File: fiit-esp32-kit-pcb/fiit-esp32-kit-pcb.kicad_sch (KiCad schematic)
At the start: 43 parts, among them J1 Conn_01x22_Pin, J2 Conn_01x22_Pin, J3 Conn_01x05_Pin, J4 Conn_01x05_Pin, J5 Conn_ARM_JTAG_SWD_10, J6 Conn_01x06_Pin, J7 QWIIC - I2C, SW5 SPST NO, U1 ESP32-S3-WROOM-1, U2 SY8089AAAC

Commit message: footprints assignment
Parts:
- removed JP1: I2C_PULL_UP, symbol Jumper:SolderJumper_3_Bridged123
- added JP1, JP2: I2C, Jumper:SolderJumper-2_P1.3mm_Bridged_RoundedPad1.0x1.5mm, symbol Jumper:SolderJumper_2_Bridged
- J1, J2: footprint (none) -> Connector_PinHeader_2.54mm:PinHeader_1x22_P2.54mm_Vertical
- J3, J4: footprint (none) -> Connector_PinHeader_2.54mm:PinHeader_1x05_P2.54mm_Vertical
- J5: footprint (none) -> Connector_IDC:IDC-Header_2x05_P2.54mm_Vertical
- J6: footprint (none) -> Connector_IDC:IDC-Header_2x03_P2.54mm_Vertical
- JP3: renamed from JP2; footprint (none) -> Jumper:SolderJumper-2_P1.3mm_Bridged_RoundedPad1.0x1.5mm
- L1: footprint Findemm:INDC2116X100N -> FIIT_Kit:INDC2116X100N
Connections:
- net +3.3V: now also JP1.2 (B), JP2.2 (B)
- net at R3.1: now also JP2.1 (A)
- net at R2.1: now also JP1.1 (A)
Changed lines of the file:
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@@
 	)
 	(junction
+		(at 246.38 110.49)
+		(diameter 0)
+		(color 0 0 0 0)
+	)
+	(junction
 		(at 163.83 168.91)
 		(diameter 0)
@@
 	(wire
 		(pts
+			(xy 238.76 113.03) (xy 238.76 110.49)
+		)
+		(stroke
+			(width 0)
+			(type default)
+		)
+	)
+	(wire
+		(pts
 			(xy 228.6 88.9) (xy 232.41 88.9)
 		)
@@
 	(wire
 		(pts
-			(xy 54.61 173.99) (xy 54.61 179.07)
+			(xy 254 113.03) (xy 254 110.49)
 		)
 		(stroke
@@
 	(wire
 		(pts
-			(xy 163.83 168.91) (xy 163.83 166.37)
+			(xy 54.61 173.99) (xy 54.61 179.07)
 		)
 		(stroke
@@
 	(wire
 		(pts
-			(xy 63.5 21.59) (xy 63.5 33.02)
+			(xy 163.83 168.91) (xy 163.83 166.37)
 		)
 		(stroke
@@
 	(wire
 		(pts
-			(xy 172.72 82.55) (xy 175.26 82.55)
+			(xy 63.5 21.59) (xy 63.5 33.02)
 		)
 		(stroke
@@
 	(wire
 		(pts
-			(xy 232.41 91.44) (xy 232.41 88.9)
+			(xy 172.72 82.55) (xy 175.26 82.55)
 		)
 		(stroke
@@
 	(wire
 		(pts
-			(xy 129.54 77.47) (xy 144.78 77.47)
+			(xy 232.41 91.44) (xy 232.41 88.9)
 		)
 		(stroke
@@
 	(wire
 		(pts
-			(xy 232.41 99.06) (xy 232.41 96.52)
+			(xy 129.54 77.47) (xy 144.78 77.47)
 		)
 		(stroke
@@
 	(wire
 		(pts
-			(xy 238.76 120.65) (xy 241.3 120.65)
+			(xy 232.41 99.06) (xy 232.41 96.52)
 		)
 		(stroke
@@
 	(wire
 		(pts
+			(xy 246.38 110.49) (xy 246.38 109.22)
+		)
+		(stroke
+			(width 0)
+			(type default)
+		)
+	)
+	(wire
+		(pts
 			(xy 142.24 29.21) (xy 144.78 29.21)
 		)
@@
 	(wire
 		(pts
+			(xy 246.38 110.49) (xy 254 110.49)
+		)
+		(stroke
+			(width 0)
+			(type default)
+		)
+	)
+	(wire
+		(pts
 			(xy 187.96 39.37) (xy 172.72 39.37)
 		)
@@
 	(wire
 		(pts
-			(xy 251.46 120.65) (xy 254 120.65)
-		)
-		(stroke
-			(width 0)
-			(type default)
-		)
-	)
-	(wire
-		(pts
 			(xy 187.96 59.69) (xy 172.72 59.69)
 		)
@@
 	(wire
 		(pts
-			(xy 246.38 115.57) (xy 246.38 116.84)
+			(xy 238.76 110.49) (xy 246.38 110.49)
 		)
 		(stroke
@@
 			)
 		)
-		(property "Footprint" "Findemm:INDC2116X100N"
+		(property "Footprint" "FIIT_Kit:INDC2116X100N"
 			(at 85.09 168.91 0)
 			(effects
@@
 	)
 	(symbol
+		(lib_id "Jumper:SolderJumper_2_Bridged")
+		(at 238.76 116.84 90)
+		(unit 1)
+		(exclude_from_sim yes)
+		(in_bom no)
+		(on_board yes)
+		(dnp no)
+		(fields_autoplaced yes)
+		(property "Reference" "JP1"
+			(at 241.3 115.5699 90)
+			(effects
+				(font
+					(size 1.27 1.27)
+				)
+				(justify right)
+			)
+		)
+		(property "Value" "I2C"
+			(at 241.3 118.1099 90)
+			(effects
+				(font
+					(size 1.27 1.27)
+				)
+				(justify right)
+			)
+		)
+		(property "Footprint" "Jumper:SolderJumper-2_P1.3mm_Bridged_RoundedPad1.0x1.5mm"
+			(at 238.76 116.84 0)
+			(effects
+				(font
+					(size 1.27 1.27)
+				)
+				(hide yes)
+			)
+		)
+		(property "Datasheet" "~"
+			(at 238.76 116.84 0)
+			(effects
+				(font
+					(size 1.27 1.27)
+				)
+				(hide yes)
+			)
+		)
+		(property "Description" "Solder Jumper, 2-pole, closed/bridged"
+			(at 238.76 116.84 0)
+			(effects
+				(font
+					(size 1.27 1.27)
+				)
+				(hide yes)
+			)
+		)
+		(pin "1"
+		)
+		(pin "2"
+		)
+		(instances
+			(project ""
+				(path "/d7013812-ce13-4db9-a6cc-42acdc5acaf9"
+					(reference "JP1")
+					(unit 1)
+				)
+			)
+		)
+	)
+	(symbol
 		(lib_id "Connector:TestPoint")
 		(at 168.91 167.64 0)
@@
 			)
 		)
-		(property "Footprint" ""
+		(property "Footprint" "Connector_PinHeader_2.54mm:PinHeader_1x22_P2.54mm_Vertical"
 			(at 167.64 54.61 0)
 			(effects
@@
 		(dnp no)
 		(fields_autoplaced yes)
-		(property "Reference" "JP2"
+		(property "Reference" "JP3"
 			(at 151.13 162.56 0)
 			(effects
@@
 			)
 		)
-		(property "Footprint" ""
+		(property "Footprint" "Jumper:SolderJumper-2_P1.3mm_Bridged_RoundedPad1.0x1.5mm"
 			(at 151.13 168.91 0)
 			(effects
@@
 			(project "fiit-esp32-kit-pcb"
 				(path "/d7013812-ce13-4db9-a6cc-42acdc5acaf9"
-					(reference "JP2")
+					(reference "JP3")
 					(unit 1)
 				)
@@
 			)
 		)
-		(property "Footprint" ""
+		(property "Footprint" "Connector_IDC:IDC-Header_2x03_P2.54mm_Vertical"
 			(at 165.1 127 0)
 			(effects
@@
 			)
 		)
-		(property "Footprint" ""
+		(property "Footprint" "Connector_PinHeader_2.54mm:PinHeader_1x22_P2.54mm_Vertical"
 			(at 149.86 54.61 0)
 			(effects
@@
 			)
 		)
-		(property "Footprint" ""
+		(property "Footprint" "Connector_PinHeader_2.54mm:PinHeader_1x05_P2.54mm_Vertical"
 			(at 223.52 93.98 0)
 			(effects
@@
 	)
 	(symbol
+		(lib_id "Jumper:SolderJumper_2_Bridged")
+		(at 254 116.84 90)
+		(unit 1)
+		(exclude_from_sim yes)
+		(in_bom no)
+		(on_board yes)
+		(dnp no)
+		(fields_autoplaced yes)
+		(property "Reference" "JP2"
+			(at 256.54 115.5699 90)
+			(effects
+				(font
+					(size 1.27 1.27)
+				)
+				(justify right)
+			)
+		)
+		(property "Value" "I2C"
+			(at 256.54 118.1099 90)
+			(effects
+				(font
+					(size 1.27 1.27)
+				)
+				(justify right)
+			)
+		)
+		(property "Footprint" "Jumper:SolderJumper-2_P1.3mm_Bridged_RoundedPad1.0x1.5mm"
+			(at 254 116.84 0)
+			(effects
+				(font
+					(size 1.27 1.27)
+				)
+				(hide yes)
+			)
+		)
+		(property "Datasheet" "~"
+			(at 254 116.84 0)
+			(effects
+				(font
+					(size 1.27 1.27)
+				)
+				(hide yes)
+			)
+		)
+		(property "Description" "Solder Jumper, 2-pole, closed/bridged"
+			(at 254 116.84 0)
+			(effects
+				(font
+					(size 1.27 1.27)
+				)
+				(hide yes)
+			)
+		)
+		(pin "1"
+		)
+		(pin "2"
+		)
+		(instances
+			(project "fiit-esp32-kit-pcb"
+				(path "/d7013812-ce13-4db9-a6cc-42acdc5acaf9"
+					(reference "JP2")
+					(unit 1)
+				)
+			)
+		)
+	)
+	(symbol
 		(lib_id "Mechanical:MountingHole")
 		(at 240.03 161.29 0)
@@
 			)
 		)
-		(property "Footprint" ""
+		(property "Footprint" "Connector_PinHeader_2.54mm:PinHeader_1x05_P2.54mm_Vertical"
 			(at 201.93 93.98 0)
 			(effects
@@
 	(symbol
 		(lib_id "power:+3.3V")
-		(at 246.38 115.57 0)
+		(at 246.38 109.22 0)
 		(unit 1)
 		(exclude_from_sim no)
@@
 		(dnp no)
 		(property "Reference" "#PWR012"
-			(at 246.38 119.38 0)
+			(at 246.38 113.03 0)
 			(effects
 				(font
@@
 		)
 		(property "Value" "+3.3V"
-			(at 246.38 111.76 0)
+			(at 246.38 105.41 0)
 			(effects
 				(font
@@
 		)
 		(property "Footprint" ""
-			(at 246.38 115.57 0)
+			(at 246.38 109.22 0)
 			(effects
 				(font
@@
 		)
 		(property "Datasheet" ""
-			(at 246.38 115.57 0)
+			(at 246.38 109.22 0)
 			(effects
 				(font
@@
 		)
 		(property "Description" "Power symbol creates a global label with name \"+3.3V\""
-			(at 246.38 115.57 0)
+			(at 246.38 109.22 0)
 			(effects
 				(font
@@
 			)
 		)
-		(property "Footprint" ""
+		(property "Footprint" "Connector_IDC:IDC-Header_2x05_P2.54mm_Vertical"
 			(at 114.3 127 0)
 			(effects
@@
 					(unit 1)
 				)
-			)
-		)
-	)
-	(symbol
-		(lib_id "Jumper:SolderJumper_3_Bridged123")
-		(at 246.38 120.65 0)
-		(mirror x)
-		(unit 1)
-		(exclude_from_sim yes)
-		(in_bom no)
-		(on_board yes)
-		(dnp no)
-		(property "Reference" "JP1"
-			(at 248.666 114.554 0)
-			(effects
-				(font
-					(size 1.27 1.27)
-				)
-			)
-		)
-		(property "Value" "I2C_PULL_UP"
-			(at 253.238 116.586 0)
-			(effects
-				(font
-					(size 1.27 1.27)
-				)
-			)
-		)
-		(property "Footprint" ""
-			(at 246.38 120.65 0)
-			(effects
-				(font
-					(size 1.27 1.27)
-				)
-				(hide yes)
-			)
-		)
-		(property "Datasheet" "~"
-			(at 246.38 120.65 0)
-			(effects
-				(font
-					(size 1.27 1.27)
-				)
-				(hide yes)
-			)
-		)
-		(property "Description" "Solder Jumper, 3-pole, pins 1+2+3 closed/bridged"
-			(at 246.38 120.65 0)
-			(effects
-				(font
-					(size 1.27 1.27)
-				)
-				(hide yes)
-			)
-		)
-		(pin "3"
-		)
-		(pin "1"
-		)
-		(pin "2"
-		)
-		(instances
-			(project ""
-				(path "/d7013812-ce13-4db9-a6cc-42acdc5acaf9"
-					(reference "JP1")
-					(unit 1)
-				)

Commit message: updated manufacturer part numbers
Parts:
- H1, H2, H3, H4: footprint MountingHole:MountingHole_3.2mm_M3 -> MountingHole:MountingHole_2.2mm_M2
- J1, J2: LCSC (none) -> C7430378; Manufacturer Part Number (none) -> DS1021-1x22SF11-B
- U1: LCSC (none) -> C2913202; Manufacturer Part Number (none) -> ESP32-S3-WROOM-1-N16R8
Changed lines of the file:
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@@
 			)
 		)
+		(property "LCSC" "~"
+			(at 238.76 116.84 0)
+			(effects
+				(font
+					(size 1.27 1.27)
+				)
+			)
+		)
+		(property "Manufacturer Part Number" "~"
+			(at 238.76 116.84 0)
+			(effects
+				(font
+					(size 1.27 1.27)
+				)
+			)
+		)
 		(pin "1"
 		)
@@
 			)
 		)
+		(property "LCSC" "C7430378"
+			(at 167.64 54.61 0)
+			(effects
+				(font
+					(size 1.27 1.27)
+				)
+				(hide yes)
+			)
+		)
+		(property "Manufacturer Part Number" "DS1021-1x22SF11-B"
+			(at 167.64 54.61 0)
+			(effects
+				(font
+					(size 1.27 1.27)
+				)
+				(hide yes)
+			)
+		)
 		(pin "1"
 		)
@@
 			)
 		)
+		(property "LCSC" "~"
+			(at 151.13 168.91 0)
+			(effects
+				(font
+					(size 1.27 1.27)
+				)
+			)
+		)
+		(property "Manufacturer Part Number" "~"
+			(at 151.13 168.91 0)
+			(effects
+				(font
+					(size 1.27 1.27)
+				)
+			)
+		)
 		(pin "1"
 		)
@@
 			)
 		)
+		(property "LCSC" "~"
+			(at 165.1 127 0)
+			(effects
+				(font
+					(size 1.27 1.27)
+				)
+			)
+		)
+		(property "Manufacturer Part Number" "~"
+			(at 165.1 127 0)
+			(effects
+				(font
+					(size 1.27 1.27)
+				)
+			)
+		)
 		(pin "1"
 		)
@@
 			)
 		)
-		(property "Footprint" "MountingHole:MountingHole_3.2mm_M3"
+		(property "Footprint" "MountingHole:MountingHole_2.2mm_M2"
 			(at 222.25 161.29 0)
 			(effects
@@
 			)
 		)
-		(property "Footprint" "MountingHole:MountingHole_3.2mm_M3"
+		(property "Footprint" "MountingHole:MountingHole_2.2mm_M2"
 			(at 222.25 156.21 0)
 			(effects
@@
 			)
 		)
+		(property "LCSC" "C7430378"
+			(at 149.86 54.61 0)
+			(effects
+				(font
+					(size 1.27 1.27)
+				)
+				(hide yes)
+			)
+		)
+		(property "Manufacturer Part Number" "DS1021-1x22SF11-B"
+			(at 149.86 54.61 0)
+			(effects
+				(font
+					(size 1.27 1.27)
+				)
+				(hide yes)
+			)
+		)
 		(pin "1"
 		)
@@
 			)
 		)
-		(property "Footprint" "MountingHole:MountingHole_3.2mm_M3"
+		(property "Footprint" "MountingHole:MountingHole_2.2mm_M2"
 			(at 240.03 156.21 0)
 			(effects
@@
 			)
 		)
+		(property "LCSC" "~"
+			(at 223.52 93.98 0)
+			(effects
+				(font
+					(size 1.27 1.27)
+				)
+			)
+		)
+		(property "Manufacturer Part Number" "~"
+			(at 223.52 93.98 0)
+			(effects
+				(font
+					(size 1.27 1.27)
+				)
+			)
+		)
 		(pin "5"
 		)
@@
 			)
 		)
+		(property "LCSC" "~"
+			(at 254 116.84 0)
+			(effects
+				(font
+					(size 1.27 1.27)
+				)
+			)
+		)
+		(property "Manufacturer Part Number" "~"
+			(at 254 116.84 0)
+			(effects
+				(font
+					(size 1.27 1.27)
+				)
+			)
+		)
 		(pin "1"
 		)
@@
 			)
 		)
-		(property "Footprint" "MountingHole:MountingHole_3.2mm_M3"
+		(property "Footprint" "MountingHole:MountingHole_2.2mm_M2"
 			(at 240.03 161.29 0)
 			(effects
@@
 			)
 		)
+		(property "LCSC" "~"
+			(at 201.93 93.98 0)
+			(effects
+				(font
+					(size 1.27 1.27)
+				)
+			)
+		)
+		(property "Manufacturer Part Number" "~"
+			(at 201.93 93.98 0)
+			(effects
+				(font
+					(size 1.27 1.27)
+				)
+			)
+		)
 		(pin "5"
 		)
@@
 			)
 		)
+		(property "LCSC" "C2913202"
+			(at 63.5 60.96 0)
+			(effects
+				(font
+					(size 1.27 1.27)
+				)
+				(hide yes)
+			)
+		)
+		(property "Manufacturer Part Number" "ESP32-S3-WROOM-1-N16R8"
+			(at 63.5 60.96 0)
+			(effects
+				(font
+					(size 1.27 1.27)
+				)
+				(hide yes)
+			)
+		)
 		(pin "1"
 		)
@@
 			)
 		)
+		(property "LCSC" "~"
+			(at 114.3 127 0)
+			(effects
+				(font
+					(size 1.27 1.27)
+				)
+			)
+		)
+		(property "Manufacturer Part Number" "~"
+			(at 114.3 127 0)
+			(effects
+				(font
+					(size 1.27 1.27)
+				)
+			)
+		)

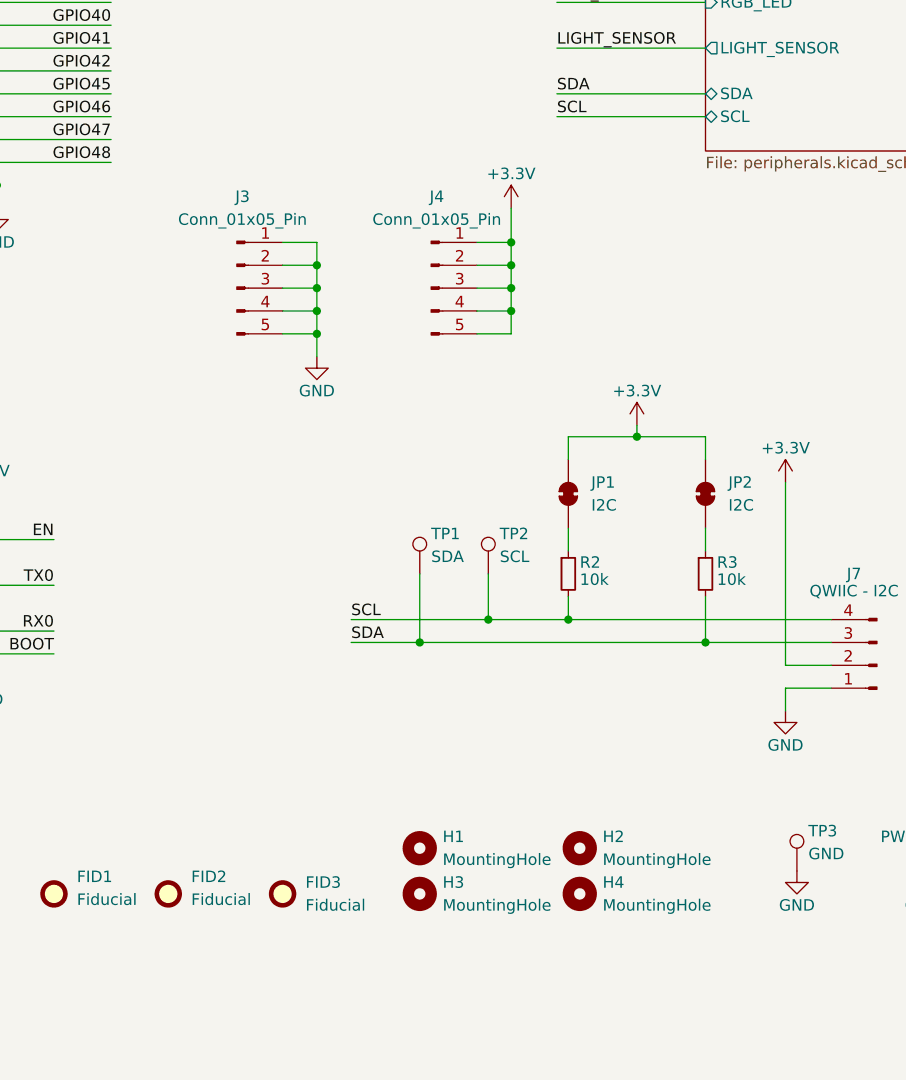
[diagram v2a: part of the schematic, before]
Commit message: component placement
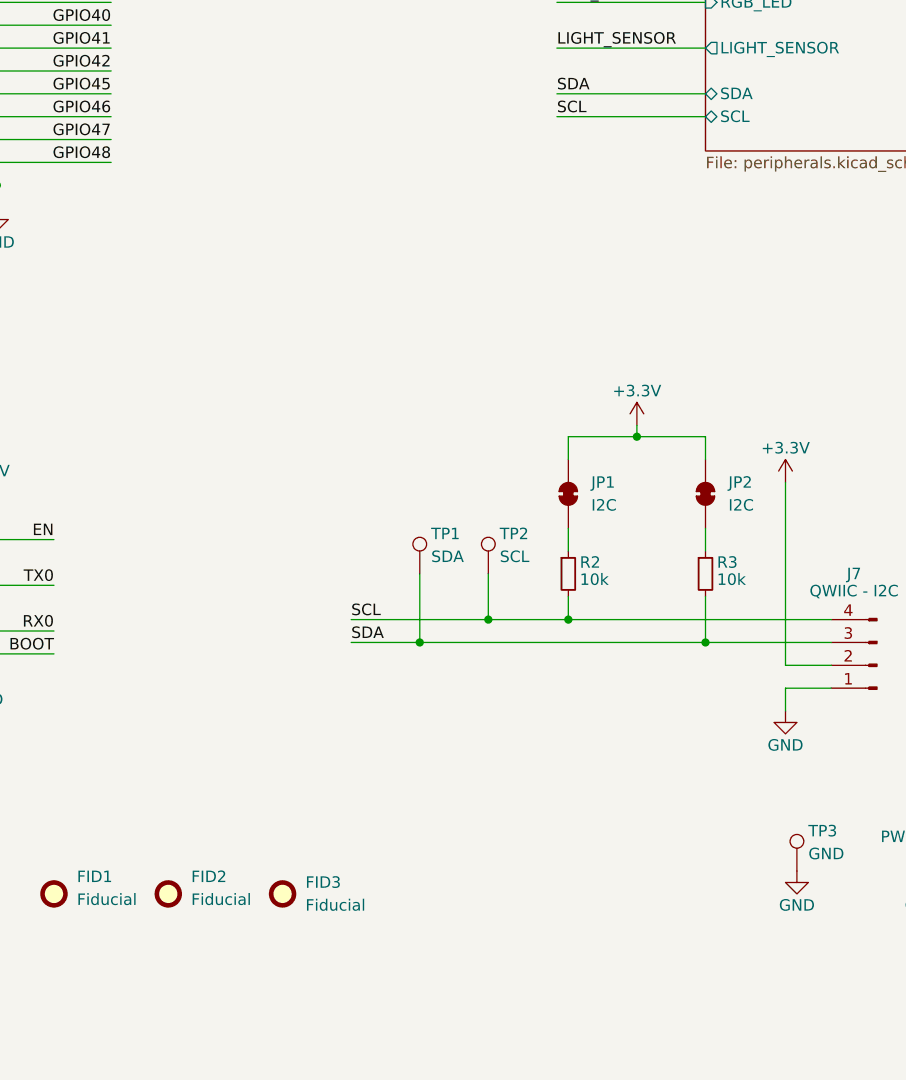
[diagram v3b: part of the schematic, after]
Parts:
- removed H1, H2, H3, H4: MountingHole, MountingHole:MountingHole_2.2mm_M2, symbol Mechanical:MountingHole
- removed J3, J4: Conn_01x05_Pin, Connector_PinHeader_2.54mm:PinHeader_1x05_P2.54mm_Vertical, symbol Connector:Conn_01x05_Pin
- SW5: footprint Button_Switch_SMD:SW_SPST_TL3342 -> Button_Switch_SMD:SW_SPST_PTS647_Sx38
- U1: LCSC C2913202 -> C2913205; Manufacturer Part Number ESP32-S3-WROOM-1-N16R8 -> ESP32-S3-WROOM-1-N16R2
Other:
- company: STU FIIT -> FIIT STU
